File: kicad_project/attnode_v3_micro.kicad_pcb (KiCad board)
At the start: 2 copper layers, 16 x 16 mm, 14 parts, among them J1 Conn_01x08_Male, J2 Conn_01x08_Male, J3 Conn_01x04_Male, U1 ATtiny3216-S

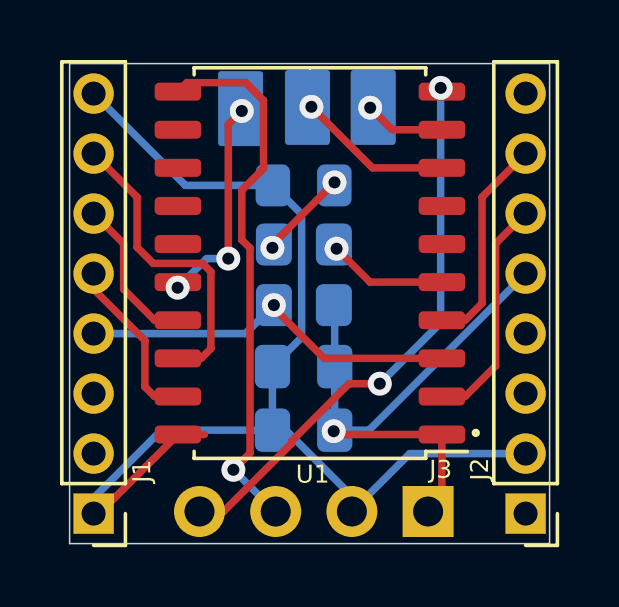
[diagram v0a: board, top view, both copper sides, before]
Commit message: Update the Boraddescription and moved the LED
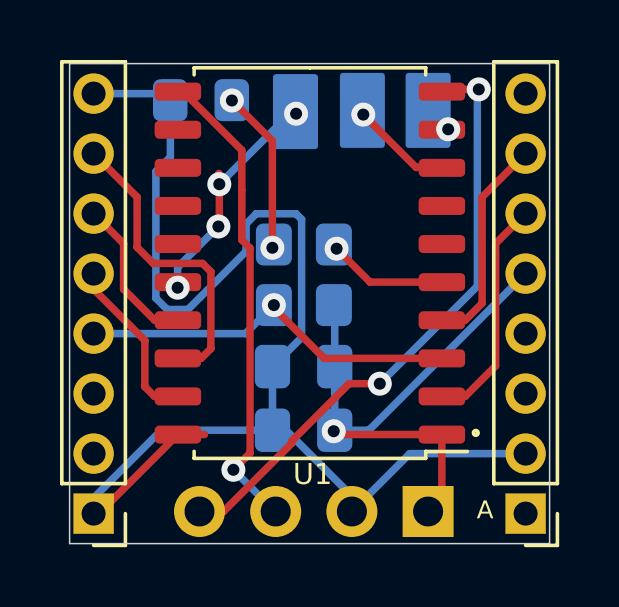
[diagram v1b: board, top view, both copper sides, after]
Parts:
- moved D1 4.45 mm to (54.4, 51.2)
- moved PRG1.3 1.83 mm to (62.0, 51.6)
- moved PRG1.1 1.83 mm to (57.5, 51.6)
- moved PRG1.2 1.83 mm to (59.8, 51.6)
- moved G*** 0.58 mm to (53.0, 61.4)
- renumbered J3 to I2C
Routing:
- net GND: track 39.1 -> 46.8 mm
- net TX: track 2.69 -> 0.00 mm
- net Net-(D1-Pad2): track 3.04 -> 5.58 mm
- net SCL: track 18.2 -> 15.9 mm
- net RX: track 5.19 -> 3.31 mm
- net SDA: track 18.5 -> 20.2 mm
- net RST: track 7.20 -> 7.59 mm, vias 3 -> 4
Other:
- board text added: "A"
- board text added: "µ-attno.de V3"
- board text removed: "J1"
- board text removed: "J2"
- board text removed: "µ-attno.de V3.0"
